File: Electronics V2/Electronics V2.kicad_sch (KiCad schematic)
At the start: 51 parts, among them J1 MOT_L, J2 MOT_R, J3 SD_Card, J4 USB_C_Receptacle_USB2.0_14P, SW1 BTN_0, SW3 RST, SW4 BOOT, SW5 BTN_1, SW6 BTN_2, SW7 BTN_3, SW8 INCR_0, U1 NCP1117-3.3_SOT223, U3 ESP32-S3-WROOM-1, U4 DAC081C081CIMK, U5 IMU_L, U6 IMU_R, U7 NCP1117-3.3_SOT223

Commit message: footprints
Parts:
- C1, C11, C12, C13, C14, C15, C16, C17, C18, C2, C3: footprint (none) -> Capacitor_SMD:C_0603_1608Metric
- R1, R10, R11, R12, R13, R14, R15, R16, R17, R18, R19, R9: footprint (none) -> Resistor_SMD:R_0603_1608Metric
- SW1, SW5, SW6, SW7: footprint (none) -> Button_Switch_SMD:SW_Push_1TS009xxxx-xxxx-xxxx_6x6x5mm
- SW3, SW4: footprint (none) -> Button_Switch_SMD:SW_Push_1P1T_NO_CK_KMR2
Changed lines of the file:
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@@
 			)
 		)
-		(property "Footprint" ""
+		(property "Footprint" "Capacitor_SMD:C_0603_1608Metric"
 			(at 105.1052 57.15 0)
 			(effects
@@
 			)
 		)
-		(property "Footprint" ""
+		(property "Footprint" "Button_Switch_SMD:SW_Push_1TS009xxxx-xxxx-xxxx_6x6x5mm"
 			(at 123.19 128.27 0)
 			(effects
@@
 			)
 		)
-		(property "Footprint" ""
+		(property "Footprint" "Button_Switch_SMD:SW_Push_1TS009xxxx-xxxx-xxxx_6x6x5mm"
 			(at 123.19 123.19 0)
 			(effects
@@
 			)
 		)
-		(property "Footprint" ""
+		(property "Footprint" "Resistor_SMD:R_0603_1608Metric"
 			(at 248.412 123.19 90)
 			(effects
@@
 			)
 		)
-		(property "Footprint" ""
+		(property "Footprint" "Resistor_SMD:R_0603_1608Metric"
 			(at 128.778 64.77 90)
 			(effects
@@
 			)
 		)
-		(property "Footprint" ""
+		(property "Footprint" "Button_Switch_SMD:SW_Push_1P1T_NO_CK_KMR2"
 			(at 109.22 53.34 0)
 			(effects
@@
 			)
 		)
-		(property "Footprint" ""
+		(property "Footprint" "Capacitor_SMD:C_0603_1608Metric"
 			(at 141.9352 149.86 0)
 			(effects
@@
 			)
 		)
-		(property "Footprint" ""
+		(property "Footprint" "Resistor_SMD:R_0603_1608Metric"
 			(at 164.592 146.05 90)
 			(effects
@@
 			)
 		)
-		(property "Footprint" ""
+		(property "Footprint" "Button_Switch_SMD:SW_Push_1TS009xxxx-xxxx-xxxx_6x6x5mm"
 			(at 123.19 118.11 0)
 			(effects
@@
 			)
 		)
-		(property "Footprint" ""
+		(property "Footprint" "Capacitor_SMD:C_0603_1608Metric"
 			(at 218.1352 147.32 0)
 			(effects
@@
 			)
 		)
-		(property "Footprint" ""
+		(property "Footprint" "Capacitor_SMD:C_0603_1608Metric"
 			(at 73.3552 177.8 0)
 			(effects
@@
 			)
 		)
-		(property "Footprint" ""
+		(property "Footprint" "Capacitor_SMD:C_0603_1608Metric"
 			(at 65.7352 177.8 0)
 			(effects
@@
 			)
 		)
-		(property "Footprint" ""
+		(property "Footprint" "Capacitor_SMD:C_0603_1608Metric"
 			(at 187.6552 149.86 0)
 			(effects
@@
 			)
 		)
-		(property "Footprint" ""
+		(property "Footprint" "Resistor_SMD:R_0603_1608Metric"
 			(at 191.262 36.83 90)
 			(effects
@@
 			)
 		)
-		(property "Footprint" ""
+		(property "Footprint" "Capacitor_SMD:C_0603_1608Metric"
 			(at 80.9752 177.8 0)
 			(effects
@@
 			)
 		)
-		(property "Footprint" ""
+		(property "Footprint" "Button_Switch_SMD:SW_Push_1P1T_NO_CK_KMR2"
 			(at 93.98 53.34 0)
 			(effects
@@
 			)
 		)
-		(property "Footprint" ""
+		(property "Footprint" "Resistor_SMD:R_0603_1608Metric"
 			(at 179.832 146.05 90)
 			(effects
@@
 			)
 		)
-		(property "Footprint" ""
+		(property "Footprint" "Resistor_SMD:R_0603_1608Metric"
 			(at 112.522 33.02 90)
 			(effects
@@
 			)
 		)
-		(property "Footprint" ""
+		(property "Footprint" "Resistor_SMD:R_0603_1608Metric"
 			(at 236.982 123.19 90)
 			(effects
@@
 			)
 		)
-		(property "Footprint" ""
+		(property "Footprint" "Capacitor_SMD:C_0603_1608Metric"
 			(at 157.1752 149.86 0)
 			(effects
@@
 			)
 		)
-		(property "Footprint" ""
+		(property "Footprint" "Resistor_SMD:R_0603_1608Metric"
 			(at 134.112 146.05 90)
 			(effects
@@
 			)
 		)
-		(property "Footprint" ""
+		(property "Footprint" "Resistor_SMD:R_0603_1608Metric"
 			(at 97.282 33.02 90)
 			(effects
@@
 			)
 		)
-		(property "Footprint" ""
+		(property "Footprint" "Capacitor_SMD:C_0603_1608Metric"
 			(at 172.4152 149.86 0)
 			(effects
@@
 			)
 		)
-		(property "Footprint" ""
+		(property "Footprint" "Resistor_SMD:R_0603_1608Metric"
 			(at 210.312 143.51 90)
 			(effects
@@
 			)
 		)
-		(property "Footprint" ""
+		(property "Footprint" "Resistor_SMD:R_0603_1608Metric"
 			(at 149.352 146.05 90)
 			(effects
@@
 			)
 		)
-		(property "Footprint" ""
+		(property "Footprint" "Capacitor_SMD:C_0603_1608Metric"
 			(at 120.3452 57.15 0)
 			(effects
@@
 			)
 		)
-		(property "Footprint" ""
+		(property "Footprint" "Button_Switch_SMD:SW_Push_1TS009xxxx-xxxx-xxxx_6x6x5mm"
 			(at 123.19 133.35 0)
 			(effects
@@
 			)
 		)
-		(property "Footprint" ""
+		(property "Footprint" "Resistor_SMD:R_0603_1608Metric"
 			(at 186.182 36.83 90)
 			(effects
@@
 			)
 		)
-		(property "Footprint" ""
+		(property "Footprint" "Capacitor_SMD:C_0603_1608Metric"
 			(at 58.1152 177.8 0)
 			(effects

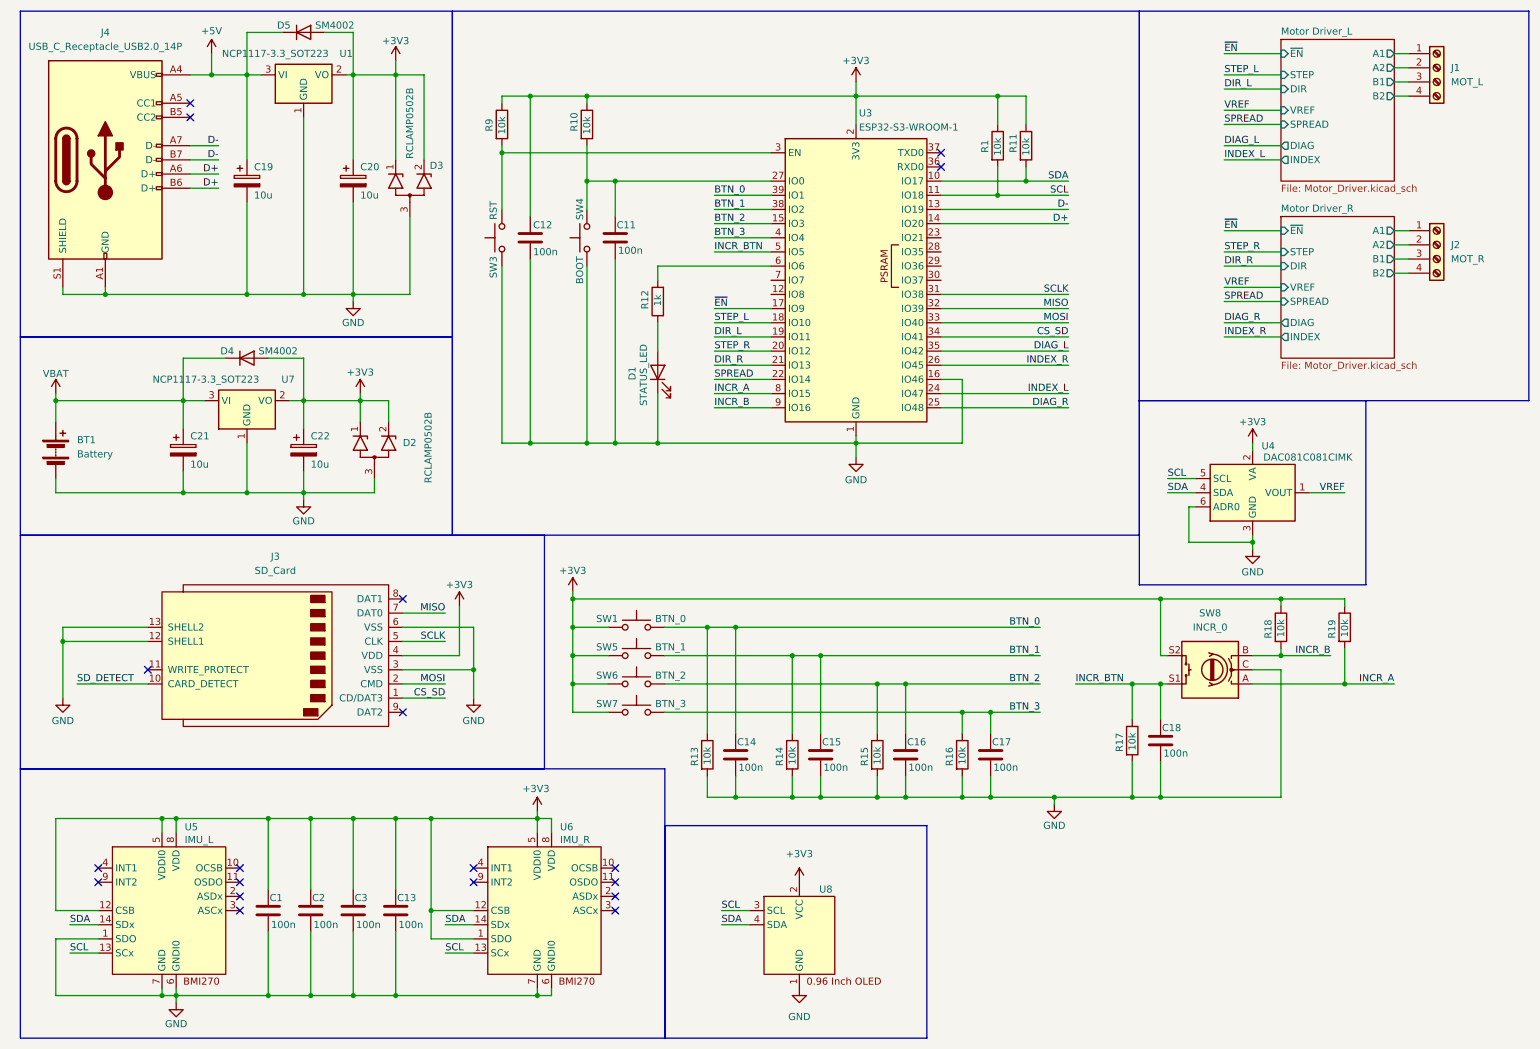
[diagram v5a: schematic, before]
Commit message: new board, needs usb, buttons, power, esd protection, transients, etc
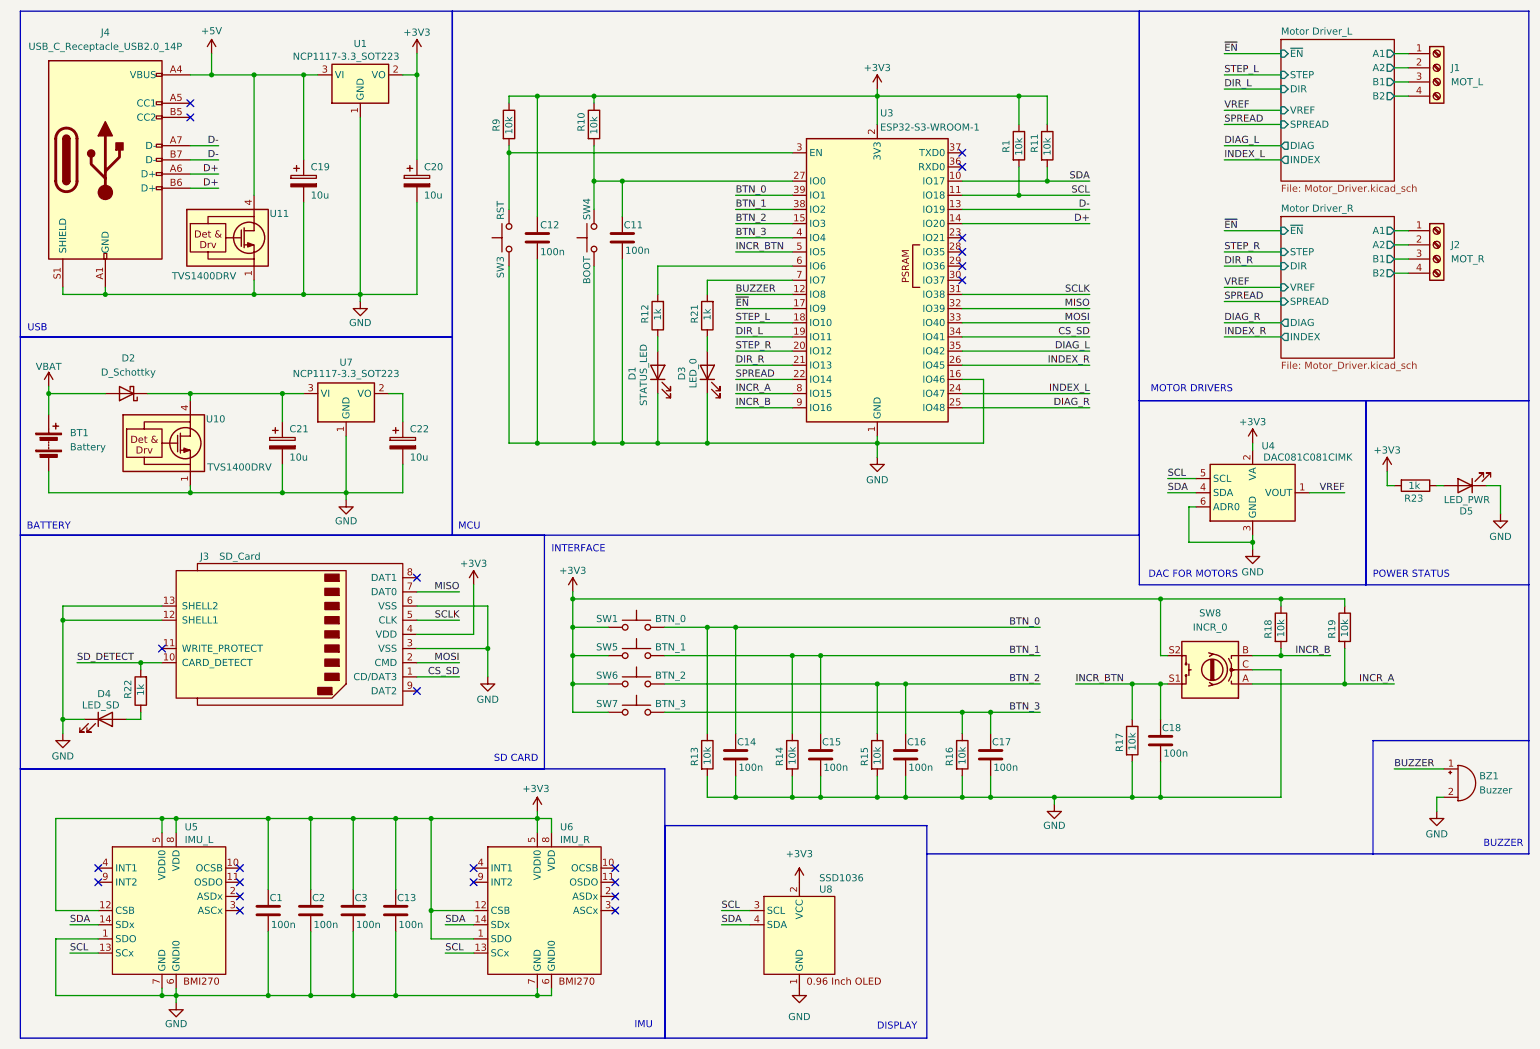
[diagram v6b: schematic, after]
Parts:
- removed D2, D3: RCLAMP0502B, Package_TO_SOT_SMD:SOT-416, symbol Power_Protection:RCLAMP0502B
- removed D4, D5: SM4002, Diode_SMD:D_MELF, symbol Diode:SM4002
- added BZ1: Buzzer, Buzzer_Beeper:Buzzer_12x9.5RM7.6, symbol Device:Buzzer
- added D2: D_Schottky, symbol Device:D_Schottky
- added D3: LED_0, LED_SMD:LED_0603_1608Metric, symbol Device:LED
- added D4: LED_SD, LED_SMD:LED_0603_1608Metric, symbol Device:LED
- added D5: LED_PWR, LED_SMD:LED_0603_1608Metric, symbol Device:LED
- added R21, R22, R23: 1k, Resistor_SMD:R_0603_1608Metric, symbol Device:R
- added U10, U11: TVS1400DRV, Package_SON:WSON-6-1EP_2x2mm_P0.65mm_EP1x1.6mm, symbol Power_Protection:TVS1400DRV
- D1: footprint (none) -> LED_SMD:LED_0603_1608Metric
- J1, J2: footprint (none) -> TerminalBlock_Phoenix:TerminalBlock_Phoenix_PT-1,5-4-3.5-H_1x04_P3.50mm_Horizontal
- J3, SW8: footprint (none) -> Connector_Card:SD_Hirose_DM1AA_SF_PEJ82
- J4: footprint (none) -> Connector_Card:SD_TE_2041021
- SW1, SW5, SW6, SW7: footprint Button_Switch_SMD:SW_Push_1TS009xxxx-xxxx-xxxx_6x6x5mm -> Button_Switch_SMD:SW_SPST_PTS645
- U8: value ~ -> SSD1036
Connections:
- net +3V3: now also R23.2; no longer C22.1, U7.2 (VO)
- net +5V: now also U11.4 (IN), U11.5 (IN), U11.6 (IN)
- net GND: now also BZ1.2 (-), D3.1 (K), D4.1 (K), D5.1 (K), U10.1 (GND), U10.2 (GND), U10.3 (GND), U10.7 (GND), U11.1 (GND), U11.2 (GND), U11.3 (GND), U11.7 (GND)
- net SD_DETECT: now also R22.2
- net VBAT: now also D2.2 (A); no longer C21.1, U7.3 (VI)
- net BUZZER: now reaches U3.12 (IO8)
- net BUZZER: now also BZ1.1 (+)
- net at U3.7 (IO7): now also R21.2
- new net: C22.1, U7.2 (VO)
- new net: C21.1, D2.1 (K), U10.4 (IN), U10.5 (IN), U10.6 (IN), U7.3 (VI)
- new net: D3.2 (A), R21.1
- new net: D4.2 (A), R22.1
- new net: D5.2 (A), R23.1
- no-connect marks 19 -> 23
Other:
- note added: "BATTERY"
- note added: "BUZZER"
- note added: "DAC FOR MOTORS"
- note added: "DISPLAY"
- note added: "IMU"
- note added: "INTERFACE"
- note added: "MCU"
- note added: "MOTOR DRIVERS"
- note added: "POWER STATUS"
- note added: "SD CARD"
- note added: "USB"
- moved on the sheet: BT1, C11, C12, C19, C20, C21, C22, J3, R1, R10, R11, R12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

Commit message: ready ro route
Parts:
- added C26, C27: 10n, Capacitor_SMD:C_0603_1608Metric, symbol Device:C
- added D6: LED_5V, LED_SMD:LED_0603_1608Metric, symbol Device:LED
- added J5: Power Probes, Connector_PinHeader_2.54mm:PinHeader_1x04_P2.54mm_Vertical, symbol Connector:Conn_01x04_Pin
- added R24: 1.5k, Resistor_SMD:R_0603_1608Metric, symbol Device:R
- added R25, R26: 10k, Resistor_SMD:R_0603_1608Metric, symbol Device:R
- D2: footprint (none) -> Rotary_Encoder:RotaryEncoder_Bourns_Vertical_PEC12R-3x17F-Sxxxx
- D5: value LED_PWR -> LED_3V3
- J4: footprint Connector_Card:SD_TE_2041021 -> Connector_USB:USB_C_Receptacle_GCT_USB4110
- SW8: footprint Connector_Card:SD_Hirose_DM1AA_SF_PEJ82 -> Rotary_Encoder:RotaryEncoder_Bourns_Vertical_PEC12R-3x17F-Sxxxx
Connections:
- net +3V3: now also J5.2 (Pin_2)
- net +5V: now also J5.1 (Pin_1), R24.2
- net GND: now also C26.2, C27.2, D6.1 (K), J5.3 (Pin_3), J5.4 (Pin_4)
- net INCR_A: now also R25.2; no longer R19.2, SW8.A
- net INCR_B: now also R26.2; no longer R18.2, SW8.B
- new net: C27.1, R19.2, R25.1, SW8.A
- new net: D6.2 (A), R24.1
- new net: C26.1, R18.2, R26.1, SW8.B
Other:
- moved on the sheet: C11, C12, D1, D3, D5, R1, R10, R11, R12, R19, R21, R23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

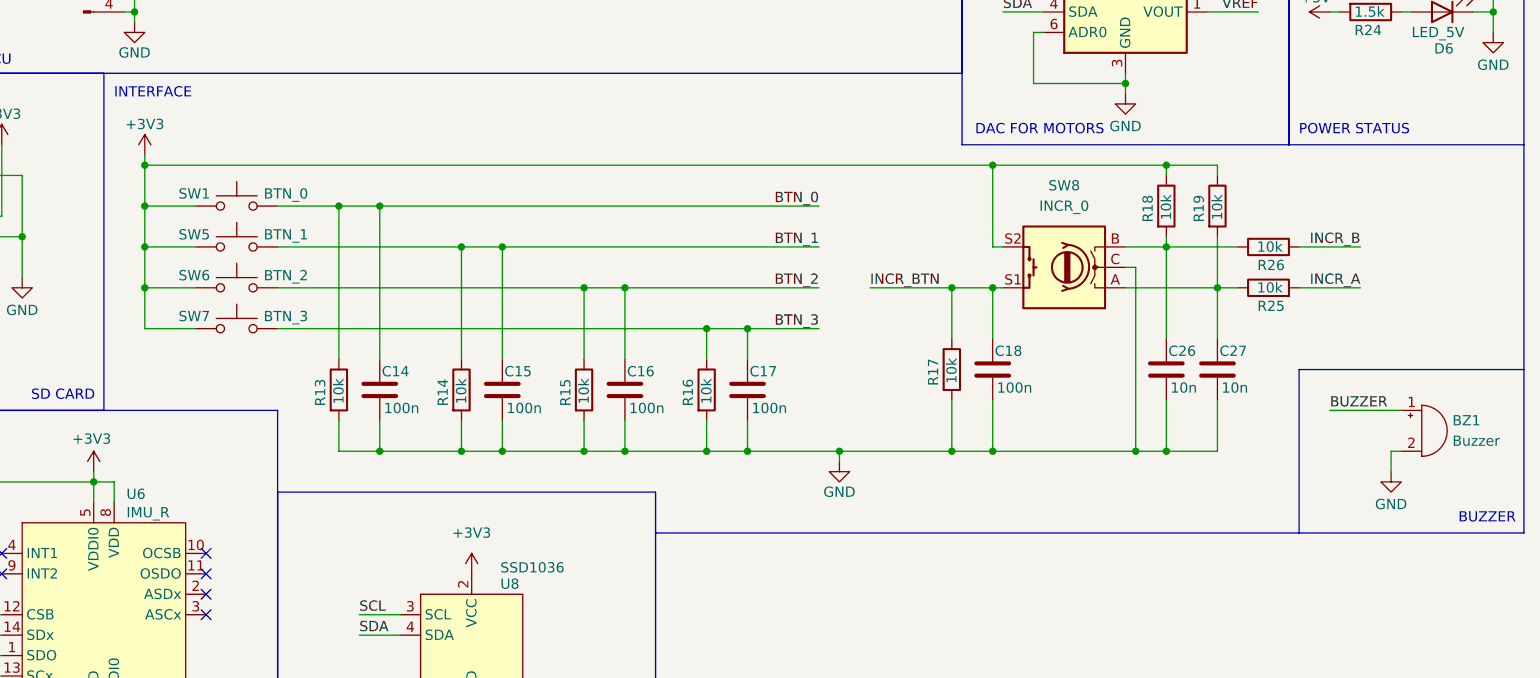
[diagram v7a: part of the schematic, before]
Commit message: bc547 alternative
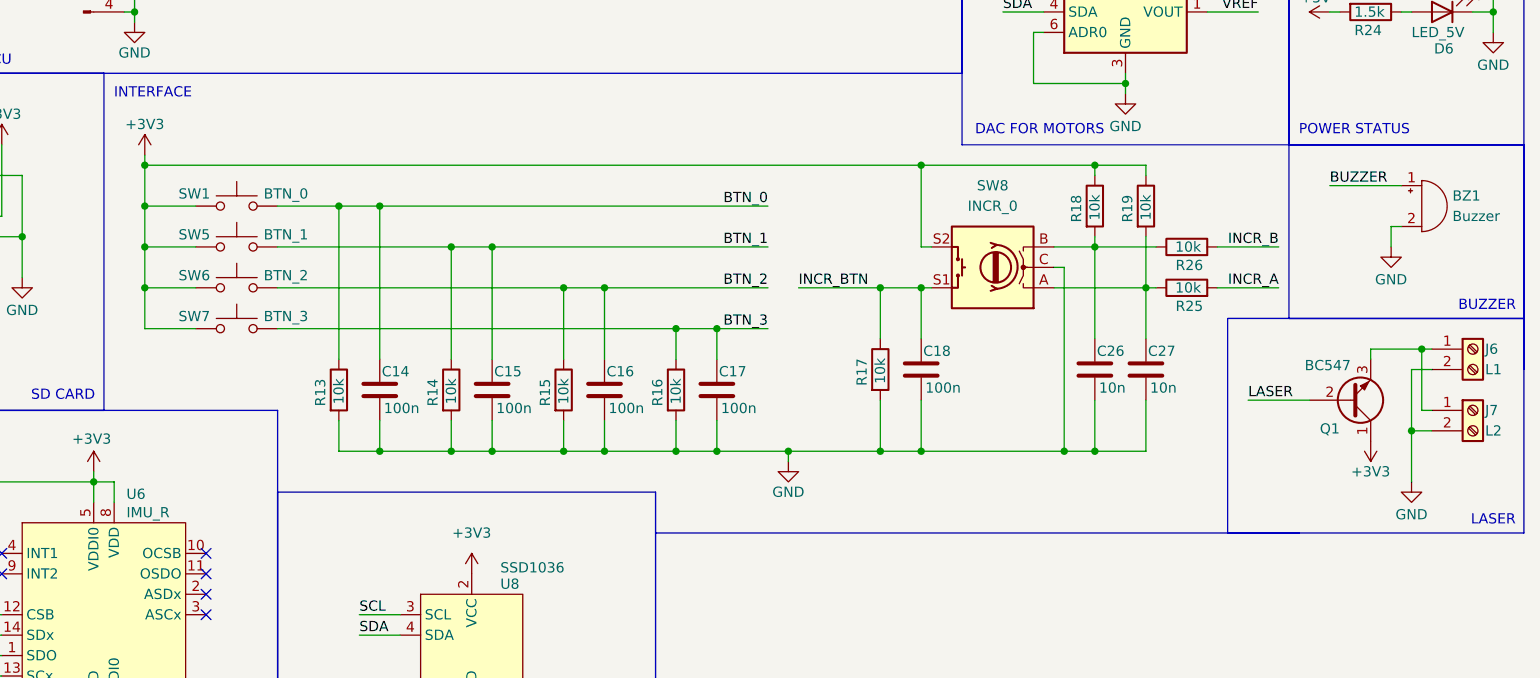
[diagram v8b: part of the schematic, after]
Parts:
- added J6: L1, TerminalBlock_Phoenix:TerminalBlock_Phoenix_PT-1,5-2-3.5-H_1x02_P3.50mm_Horizontal, symbol Connector:Screw_Terminal_01x02
- added J7: L2, TerminalBlock_Phoenix:TerminalBlock_Phoenix_PT-1,5-2-3.5-H_1x02_P3.50mm_Horizontal, symbol Connector:Screw_Terminal_01x02
- added Q1: BC547, Package_TO_SOT_THT:TO-92_Inline, symbol Transistor_BJT:BC547
- D2: footprint Rotary_Encoder:RotaryEncoder_Bourns_Vertical_PEC12R-3x17F-Sxxxx -> Package_TO_SOT_SMD:TO-277A
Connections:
- net +3V3: now also Q1.1 (C)
- net GND: now also J6.2 (Pin_2), J7.2 (Pin_2)
- new net: J6.1 (Pin_1), J7.1 (Pin_1), Q1.3 (E)
- new net LASER: Q1.2 (B)
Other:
- note added: "LASER"
- moved on the sheet: BZ1, C15, C16, C17, C18, C26, C27, R14, R15, R16, R17, R18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
